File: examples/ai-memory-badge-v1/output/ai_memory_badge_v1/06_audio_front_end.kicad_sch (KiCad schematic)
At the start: 7 parts

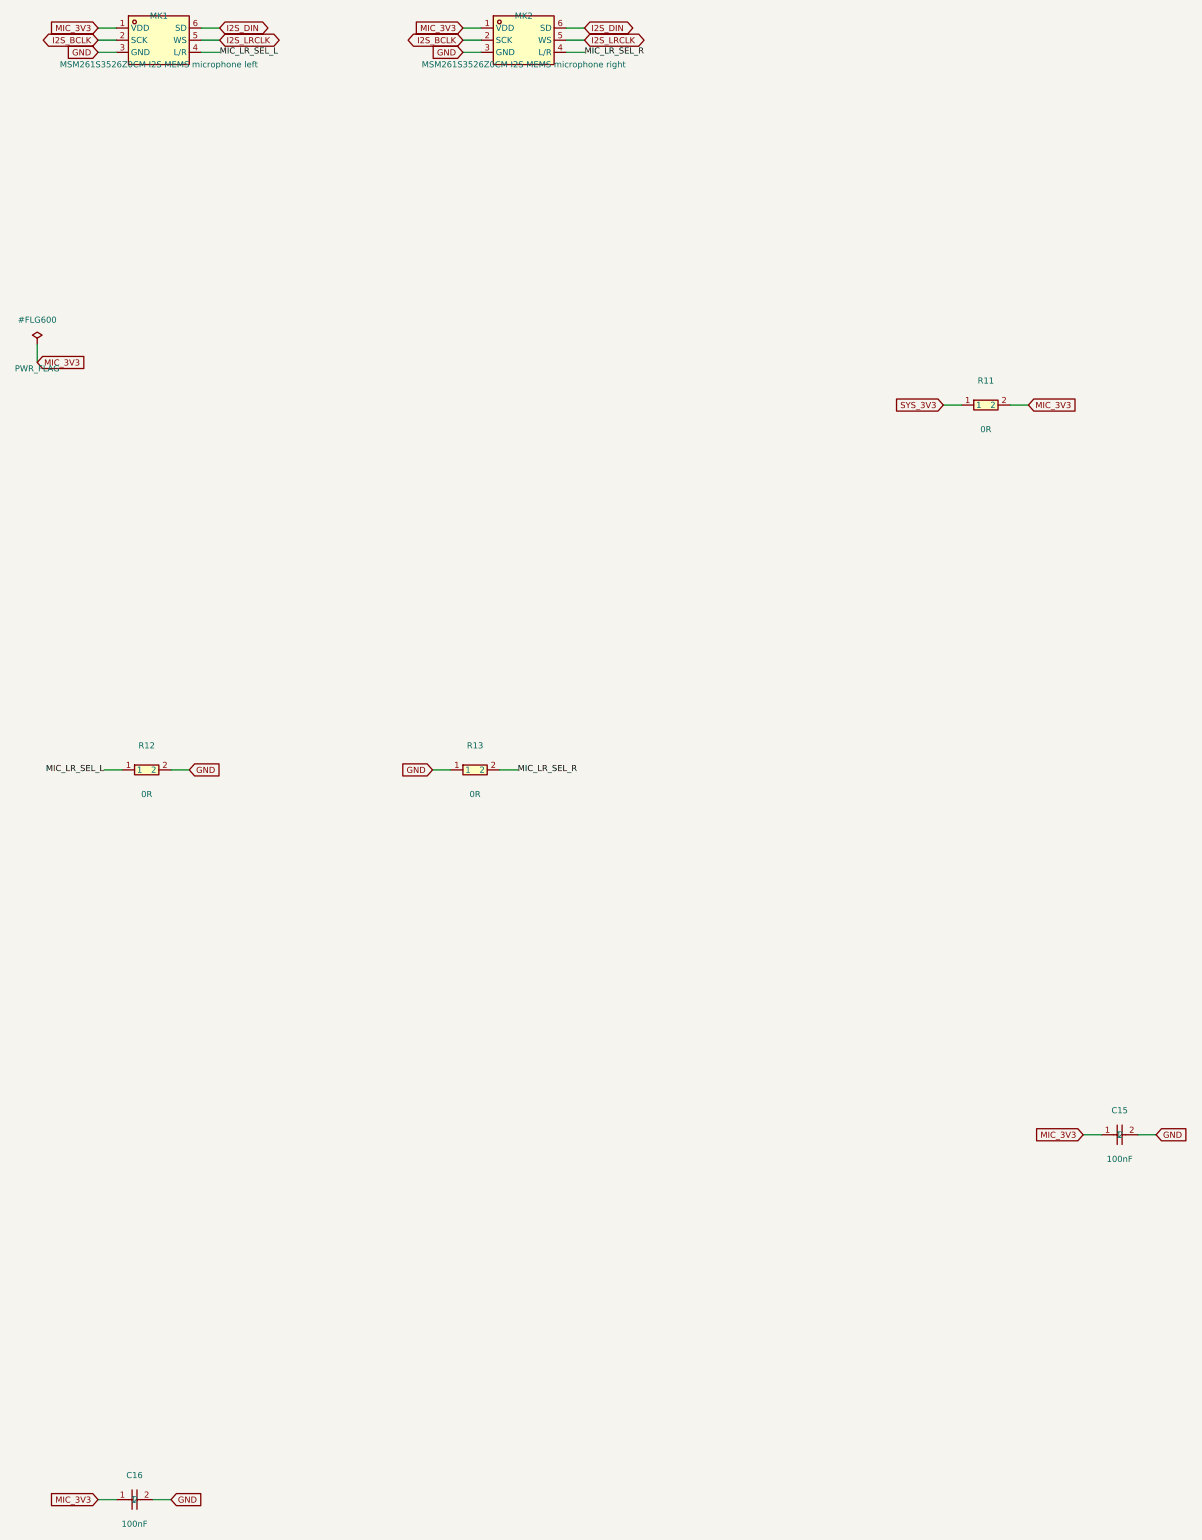
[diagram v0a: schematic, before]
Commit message: feat: split schematic layout from PCB placement / 将原理图布局与PCB摆位分离
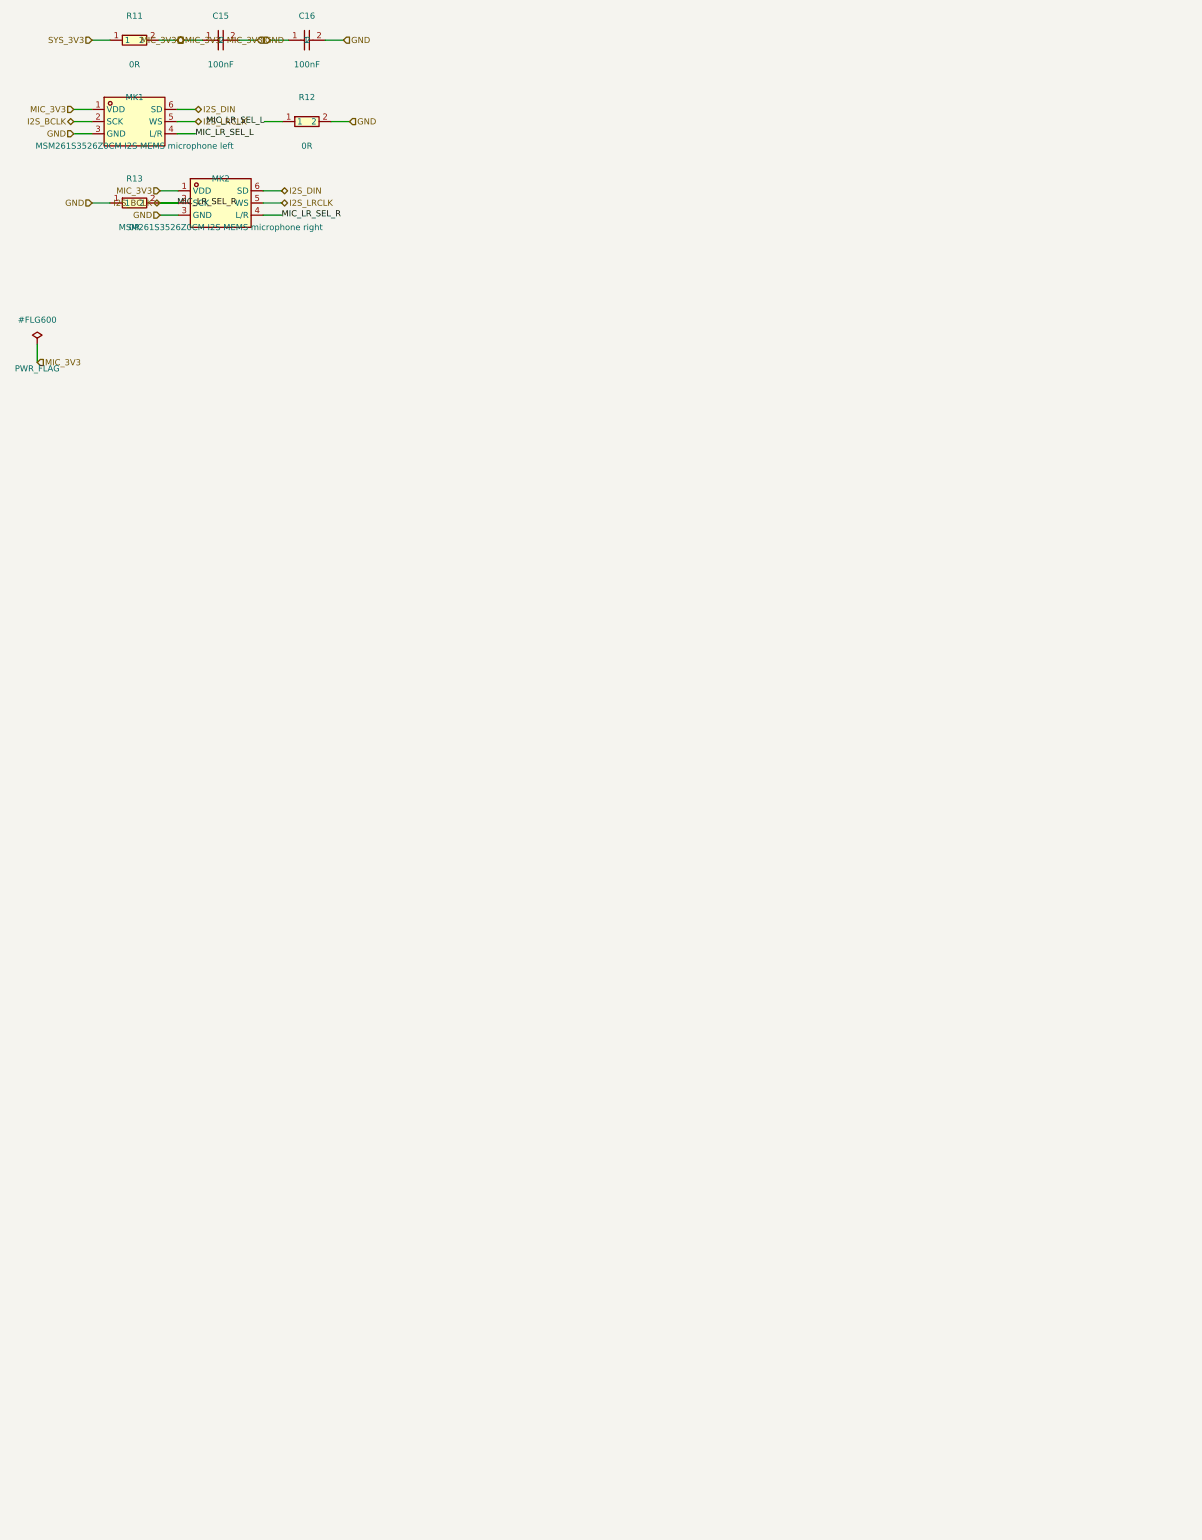
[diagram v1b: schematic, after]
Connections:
- net MIC_LR_SEL_R is gone; now on net I2S_BCLK: MK2.4 (L/R), R13.2
